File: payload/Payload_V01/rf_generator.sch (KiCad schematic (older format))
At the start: 39 parts, among them J1 Screw_Terminal_01x02, J2 Screw_Terminal_01x02, J3 Conn_Coaxial, J4 Conn_Coaxial, J5 Conn_Coaxial, U1 REF196, U2 AD9838, Y1 SG-310SCF

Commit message: added footprints and 3d models
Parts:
- JP1, JP3, JP4: footprint (none) -> Jumper:SolderJumper-3_P1.3mm_Open_Pad1.0x1.5mm
- JP2: footprint (none) -> Jumper:SolderJumper-2_P1.3mm_Bridged2Bar_Pad1.0x1.5mm
- U1: footprint (none) -> Package_SO:TSSOP-8_4.4x3mm_P0.65mm
- Y1: footprint (none) -> Crystal:Crystal_SMD_SeikoEpson_TSX3225-4Pin_3.2x2.5mm_HandSoldering
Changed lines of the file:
@@
 F 0 "JP2" H 4950 3014 50  0000 C CNN
 F 1 "Jumper" H 4950 2923 50  0000 C CNN
-F 2 "" H 4950 2750 50  0001 C CNN
+F 2 "Jumper:SolderJumper-2_P1.3mm_Bridged2Bar_Pad1.0x1.5mm" H 4950 2750 50  0001 C CNN
 F 3 "~" H 4950 2750 50  0001 C CNN
 	1    4950 2750
@@
 F 0 "JP3" H 5250 1674 50  0000 C CNN
 F 1 "Jumper_3_Open" H 5250 1583 50  0000 C CNN
-F 2 "" H 5250 1450 50  0001 C CNN
+F 2 "Jumper:SolderJumper-3_P1.3mm_Open_Pad1.0x1.5mm" H 5250 1450 50  0001 C CNN
 F 3 "~" H 5250 1450 50  0001 C CNN
 	1    5250 1450
@@
 F 0 "JP4" H 6100 1674 50  0000 C CNN
 F 1 "Jumper_3_Open" H 6100 1583 50  0000 C CNN
-F 2 "" H 6100 1450 50  0001 C CNN
+F 2 "Jumper:SolderJumper-3_P1.3mm_Open_Pad1.0x1.5mm" H 6100 1450 50  0001 C CNN
 F 3 "~" H 6100 1450 50  0001 C CNN
 	1    6100 1450
@@
 F 0 "Y1" H 3225 6125 50  0000 C CNN
 F 1 "SG-310SCF" H 3225 6034 50  0000 C CNN
-F 2 "" H 3200 5700 50  0001 C CNN
+F 2 "Crystal:Crystal_SMD_SeikoEpson_TSX3225-4Pin_3.2x2.5mm_HandSoldering" H 3200 5700 50  0001 C CNN
 F 3 "" H 3200 5700 50  0001 C CNN
 	1    3200 5700
@@
 F 0 "JP1" V 2596 5587 50  0000 L CNN
 F 1 "Jumper_3_Open" V 2505 5587 50  0000 L CNN
-F 2 "" H 2550 5500 50  0001 C CNN
+F 2 "Jumper:SolderJumper-3_P1.3mm_Open_Pad1.0x1.5mm" H 2550 5500 50  0001 C CNN
 F 3 "~" H 2550 5500 50  0001 C CNN
 	1    2550 5500
@@
 F 0 "U1" H 2644 6696 50  0000 L CNN
 F 1 "REF196" H 2350 6400 50  0000 L CNN
-F 2 "" H 2300 6600 50  0001 C CIN
+F 2 "Package_SO:TSSOP-8_4.4x3mm_P0.65mm" H 2300 6600 50  0001 C CIN
 F 3 "https://www.analog.com/static/imported-files/data_sheets/REF19xSeries.pdf" H 2300 6600 50  0001 C CIN
 	1    2300 6650

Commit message: some changes to schematics
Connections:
- net VDDA is gone; now on net +3V3: C3.1, C5.1, J1.1 (Pin_1), JP4.1 (A)
- net VDD renamed +3V3
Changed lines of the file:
@@
 Wire Wire Line
 	4750 1450 4750 1250
-$Comp
-L power:VDD #PWR?
-U 1 1 5F1B5F0C
-P 4750 1250
-AR Path="/5F1B5F0C" Ref="#PWR?"  Part="1"
-AR Path="/5F190638/5F1B5F0C" Ref="#PWR0101"  Part="1"
-F 0 "#PWR0101" H 4750 1100 50  0001 C CNN
-F 1 "VDD" H 4765 1423 50  0000 C CNN
-F 2 "" H 4750 1250 50  0001 C CNN
-F 3 "" H 4750 1250 50  0001 C CNN
-	1    4750 1250
-	1    0    0    -1
-$EndComp
 Wire Wire Line
 	5500 1450 5700 1450
@@
 Wire Wire Line
 	5850 1450 5850 1200
-$Comp
-L power:VDDA #PWR?
-U 1 1 5F1B5F1E
-P 5850 1200
-AR Path="/5F1B5F1E" Ref="#PWR?"  Part="1"
-AR Path="/5F190638/5F1B5F1E" Ref="#PWR0102"  Part="1"
-F 0 "#PWR0102" H 5850 1050 50  0001 C CNN
-F 1 "VDDA" H 5865 1373 50  0000 C CNN
-F 2 "" H 5850 1200 50  0001 C CNN
-F 3 "" H 5850 1200 50  0001 C CNN
-	1    5850 1200
-	1    0    0    -1
-$EndComp
 $Comp
 L Device:C C?
@@
 Wire Wire Line
 	9150 5700 9150 5800
-$Comp
-L power:GNDD #PWR?
-U 1 1 5F1B5FEE
-P 4650 5950
-AR Path="/5F1B5FEE" Ref="#PWR?"  Part="1"
-AR Path="/5F190638/5F1B5FEE" Ref="#PWR0114"  Part="1"
-F 0 "#PWR0114" H 4650 5700 50  0001 C CNN
-F 1 "GNDD" H 4654 5795 50  0000 C CNN
-F 2 "" H 4650 5950 50  0001 C CNN
-F 3 "" H 4650 5950 50  0001 C CNN
-	1    4650 5950
-	1    0    0    -1
-$EndComp
 Wire Wire Line
 	4650 5950 4650 5850
@@
 Wire Wire Line
 	3800 5900 3800 6000
-$Comp
-L power:GNDD #PWR?
-U 1 1 5F1B600A
-P 3800 6000
-AR Path="/5F1B600A" Ref="#PWR?"  Part="1"
-AR Path="/5F190638/5F1B600A" Ref="#PWR0115"  Part="1"
-F 0 "#PWR0115" H 3800 5750 50  0001 C CNN
-F 1 "GNDD" H 3804 5845 50  0000 C CNN
-F 2 "" H 3800 6000 50  0001 C CNN
-F 3 "" H 3800 6000 50  0001 C CNN
-	1    3800 6000
-	1    0    0    -1
-$EndComp
 Wire Wire Line
 	2900 5900 2750 5900
@@
 Wire Wire Line
 	2550 5250 2550 5150
-$Comp
-L power:VDD #PWR?
-U 1 1 5F1B6019
-P 2550 5150
-AR Path="/5F1B6019" Ref="#PWR?"  Part="1"
-AR Path="/5F190638/5F1B6019" Ref="#PWR0116"  Part="1"
-F 0 "#PWR0116" H 2550 5000 50  0001 C CNN
-F 1 "VDD" H 2565 5323 50  0000 C CNN
-F 2 "" H 2550 5150 50  0001 C CNN
-F 3 "" H 2550 5150 50  0001 C CNN
-	1    2550 5150
-	1    0    0    -1
-$EndComp
 Wire Wire Line
 	4000 5200 4250 5200
@@
 	1250 6950 1250 7050
 Connection ~ 1250 6950
-$Comp
-L power:GNDD #PWR?
-U 1 1 5F1B602F
-P 1250 7050
-AR Path="/5F1B602F" Ref="#PWR?"  Part="1"
-AR Path="/5F190638/5F1B602F" Ref="#PWR0117"  Part="1"
-F 0 "#PWR0117" H 1250 6800 50  0001 C CNN
-F 1 "GNDD" H 1254 6895 50  0000 C CNN
-F 2 "" H 1250 7050 50  0001 C CNN
-F 3 "" H 1250 7050 50  0001 C CNN
-	1    1250 7050
-	1    0    0    -1
-$EndComp
 Wire Wire Line
 	1250 6650 1500 6650
@@
 Wire Wire Line
 	2900 6950 3200 6950
-$Comp
-L power:GNDD #PWR?
-U 1 1 5F1B6046
-P 2900 7050
-AR Path="/5F1B6046" Ref="#PWR?"  Part="1"
-AR Path="/5F190638/5F1B6046" Ref="#PWR0118"  Part="1"
-F 0 "#PWR0118" H 2900 6800 50  0001 C CNN
-F 1 "GNDD" H 2904 6895 50  0000 C CNN
-F 2 "" H 2900 7050 50  0001 C CNN
-F 3 "" H 2900 7050 50  0001 C CNN
-	1    2900 7050
-	1    0    0    -1
-$EndComp
-$Comp
-L power:GNDD #PWR?
-U 1 1 5F1B604C
-P 2300 7050
-AR Path="/5F1B604C" Ref="#PWR?"  Part="1"
-AR Path="/5F190638/5F1B604C" Ref="#PWR0119"  Part="1"
-F 0 "#PWR0119" H 2300 6800 50  0001 C CNN
-F 1 "GNDD" H 2304 6895 50  0000 C CNN
-F 2 "" H 2300 7050 50  0001 C CNN
-F 3 "" H 2300 7050 50  0001 C CNN
-	1    2300 7050
-	1    0    0    -1
-$EndComp
 Wire Wire Line
 	2300 7050 2300 6950
@@
 $EndComp
 $Comp
-L power:VDD #PWR?
-U 1 1 5F1B609E
-P 1450 1200
-AR Path="/5F1B609E" Ref="#PWR?"  Part="1"
-AR Path="/5F190638/5F1B609E" Ref="#PWR0120"  Part="1"
-F 0 "#PWR0120" H 1450 1050 50  0001 C CNN
-F 1 "VDD" H 1465 1373 50  0000 C CNN
-F 2 "" H 1450 1200 50  0001 C CNN
-F 3 "" H 1450 1200 50  0001 C CNN
-	1    1450 1200
-	1    0    0    -1
-$EndComp
-$Comp
-L power:VDDA #PWR?
-U 1 1 5F1B60A4
-P 1400 2150
-AR Path="/5F1B60A4" Ref="#PWR?"  Part="1"
-AR Path="/5F190638/5F1B60A4" Ref="#PWR0121"  Part="1"
-F 0 "#PWR0121" H 1400 2000 50  0001 C CNN
-F 1 "VDDA" H 1415 2323 50  0000 C CNN
-F 2 "" H 1400 2150 50  0001 C CNN
-F 3 "" H 1400 2150 50  0001 C CNN
-	1    1400 2150
-	1    0    0    -1
-$EndComp
-$Comp
 L Device:C C?
 U 1 1 5F1B60AA
@@
 $EndComp
 $Comp
-L power:GNDD #PWR?
-U 1 1 5F1B60C2
-P 1450 1600
-AR Path="/5F1B60C2" Ref="#PWR?"  Part="1"
-AR Path="/5F190638/5F1B60C2" Ref="#PWR0122"  Part="1"
-F 0 "#PWR0122" H 1450 1350 50  0001 C CNN
-F 1 "GNDD" H 1454 1445 50  0000 C CNN
-F 2 "" H 1450 1600 50  0001 C CNN
-F 3 "" H 1450 1600 50  0001 C CNN
-	1    1450 1600
-	1    0    0    -1
-$EndComp
-$Comp
 L power:GND #PWR?
 U 1 1 5F1B60C8
@@
 	2150 1250 2700 1250
 $Comp
-L power:GNDD #PWR?
-U 1 1 5F1B60EB
-P 4150 2300
-AR Path="/5F1B60EB" Ref="#PWR?"  Part="1"
-AR Path="/5F190638/5F1B60EB" Ref="#PWR0124"  Part="1"
-F 0 "#PWR0124" H 4150 2050 50  0001 C CNN
-F 1 "GNDD" H 4154 2145 50  0000 C CNN
-F 2 "" H 4150 2300 50  0001 C CNN
-F 3 "" H 4150 2300 50  0001 C CNN
-	1    4150 2300
-	1    0    0    -1
-$EndComp
-$Comp
-L power:GNDD #PWR?
-U 1 1 5F1B60F1
-P 3900 3150
-AR Path="/5F1B60F1" Ref="#PWR?"  Part="1"
-AR Path="/5F190638/5F1B60F1" Ref="#PWR0125"  Part="1"
-F 0 "#PWR0125" H 3900 2900 50  0001 C CNN
-F 1 "GNDD" H 3904 2995 50  0000 C CNN
-F 2 "" H 3900 3150 50  0001 C CNN
-F 3 "" H 3900 3150 50  0001 C CNN
-	1    3900 3150
-	1    0    0    -1
-$EndComp
-Connection ~ 3900 3150
-$Comp
 L power:GND #PWR?
 U 1 1 5F1B60F8
@@
 Text Notes 8050 7000 0    197  ~ 39
 RF Generator
+$Comp
+L power:+3V3 #PWR?
+U 1 1 5F2F2E43
+P 2550 5150
+F 0 "#PWR?" H 2550 5000 50  0001 C CNN
+F 1 "+3V3" H 2565 5323 50  0000 C CNN
+F 2 "" H 2550 5150 50  0001 C CNN
+F 3 "" H 2550 5150 50  0001 C CNN
+	1    2550 5150
+	1    0    0    -1
+$EndComp
+$Comp
+L power:+3V3 #PWR?
+U 1 1 5F2F3260
+P 1400 2150
+F 0 "#PWR?" H 1400 2000 50  0001 C CNN
+F 1 "+3V3" H 1415 2323 50  0000 C CNN
+F 2 "" H 1400 2150 50  0001 C CNN
+F 3 "" H 1400 2150 50  0001 C CNN
+	1    1400 2150
+	1    0    0    -1
+$EndComp
+$Comp
+L power:+3V3 #PWR?
+U 1 1 5F2F483A
+P 1450 1200
+F 0 "#PWR?" H 1450 1050 50  0001 C CNN
+F 1 "+3V3" H 1465 1373 50  0000 C CNN
+F 2 "" H 1450 1200 50  0001 C CNN
+F 3 "" H 1450 1200 50  0001 C CNN
+	1    1450 1200
+	1    0    0    -1
+$EndComp
+$Comp
+L power:+3V3 #PWR?
+U 1 1 5F2F4AD5
+P 4750 1250
+F 0 "#PWR?" H 4750 1100 50  0001 C CNN
+F 1 "+3V3" H 4765 1423 50  0000 C CNN
+F 2 "" H 4750 1250 50  0001 C CNN
+F 3 "" H 4750 1250 50  0001 C CNN
+	1    4750 1250
+	1    0    0    -1
+$EndComp
+$Comp
+L power:+3V3 #PWR?
+U 1 1 5F2F4E73
+P 5850 1200
+F 0 "#PWR?" H 5850 1050 50  0001 C CNN
+F 1 "+3V3" H 5865 1373 50  0000 C CNN
+F 2 "" H 5850 1200 50  0001 C CNN
+F 3 "" H 5850 1200 50  0001 C CNN
+	1    5850 1200
+	1    0    0    -1
+$EndComp
+$Comp
+L power:GND #PWR?
+U 1 1 5F2F56C1
+P 3800 6000
+AR Path="/5F2F56C1" Ref="#PWR?"  Part="1"
+AR Path="/5F190638/5F2F56C1" Ref="#PWR?"  Part="1"
+F 0 "#PWR?" H 3800 5750 50  0001 C CNN
+F 1 "GND" H 3805 5827 50  0000 C CNN
+F 2 "" H 3800 6000 50  0001 C CNN
+F 3 "" H 3800 6000 50  0001 C CNN
+	1    3800 6000
+	1    0    0    -1
+$EndComp
+$Comp
+L power:GND #PWR?
+U 1 1 5F2F58CD
+P 2900 7050
+AR Path="/5F2F58CD" Ref="#PWR?"  Part="1"
+AR Path="/5F190638/5F2F58CD" Ref="#PWR?"  Part="1"
+F 0 "#PWR?" H 2900 6800 50  0001 C CNN
+F 1 "GND" H 2905 6877 50  0000 C CNN
+F 2 "" H 2900 7050 50  0001 C CNN
+F 3 "" H 2900 7050 50  0001 C CNN
+	1    2900 7050
+	1    0    0    -1
+$EndComp
+$Comp
+L power:GND #PWR?
+U 1 1 5F2F5C8A
+P 2300 7050
+AR Path="/5F2F5C8A" Ref="#PWR?"  Part="1"
+AR Path="/5F190638/5F2F5C8A" Ref="#PWR?"  Part="1"
+F 0 "#PWR?" H 2300 6800 50  0001 C CNN
+F 1 "GND" H 2305 6877 50  0000 C CNN
+F 2 "" H 2300 7050 50  0001 C CNN
+F 3 "" H 2300 7050 50  0001 C CNN
+	1    2300 7050
+	1    0    0    -1
+$EndComp
+$Comp
+L power:GND #PWR?
+U 1 1 5F2F5EE7
+P 1250 7050
+AR Path="/5F2F5EE7" Ref="#PWR?"  Part="1"
+AR Path="/5F190638/5F2F5EE7" Ref="#PWR?"  Part="1"
+F 0 "#PWR?" H 1250 6800 50  0001 C CNN
+F 1 "GND" H 1255 6877 50  0000 C CNN
+F 2 "" H 1250 7050 50  0001 C CNN
+F 3 "" H 1250 7050 50  0001 C CNN
+	1    1250 7050
+	1    0    0    -1
+$EndComp
+$Comp
+L power:GND #PWR?
+U 1 1 5F2F65B3
+P 4650 5950
+AR Path="/5F2F65B3" Ref="#PWR?"  Part="1"
+AR Path="/5F190638/5F2F65B3" Ref="#PWR?"  Part="1"
+F 0 "#PWR?" H 4650 5700 50  0001 C CNN
+F 1 "GND" H 4655 5777 50  0000 C CNN
+F 2 "" H 4650 5950 50  0001 C CNN
+F 3 "" H 4650 5950 50  0001 C CNN
+	1    4650 5950
+	1    0    0    -1
+$EndComp
+$Comp
+L power:GND #PWR?
+U 1 1 5F2F6675
+P 3900 3150
+AR Path="/5F2F6675" Ref="#PWR?"  Part="1"
+AR Path="/5F190638/5F2F6675" Ref="#PWR?"  Part="1"
+F 0 "#PWR?" H 3900 2900 50  0001 C CNN
+F 1 "GND" H 3905 2977 50  0000 C CNN
+F 2 "" H 3900 3150 50  0001 C CNN
+F 3 "" H 3900 3150 50  0001 C CNN
+	1    3900 3150
+	1    0    0    -1
+$EndComp
+Connection ~ 3900 3150
+$Comp
+L power:GND #PWR?
+U 1 1 5F2F6AE6
+P 4150 2300
+AR Path="/5F2F6AE6" Ref="#PWR?"  Part="1"
+AR Path="/5F190638/5F2F6AE6" Ref="#PWR?"  Part="1"
+F 0 "#PWR?" H 4150 2050 50  0001 C CNN
+F 1 "GND" H 4155 2127 50  0000 C CNN
+F 2 "" H 4150 2300 50  0001 C CNN
+F 3 "" H 4150 2300 50  0001 C CNN
+	1    4150 2300
+	1    0    0    -1
+$EndComp
+$Comp
+L power:GND #PWR?
+U 1 1 5F2F6E6D
+P 1450 1600
+AR Path="/5F2F6E6D" Ref="#PWR?"  Part="1"
+AR Path="/5F190638/5F2F6E6D" Ref="#PWR?"  Part="1"
+F 0 "#PWR?" H 1450 1350 50  0001 C CNN
+F 1 "GND" H 1455 1427 50  0000 C CNN
+F 2 "" H 1450 1600 50  0001 C CNN
+F 3 "" H 1450 1600 50  0001 C CNN
+	1    1450 1600
+	1    0    0    -1
+$EndComp
 $EndSCHEMATC

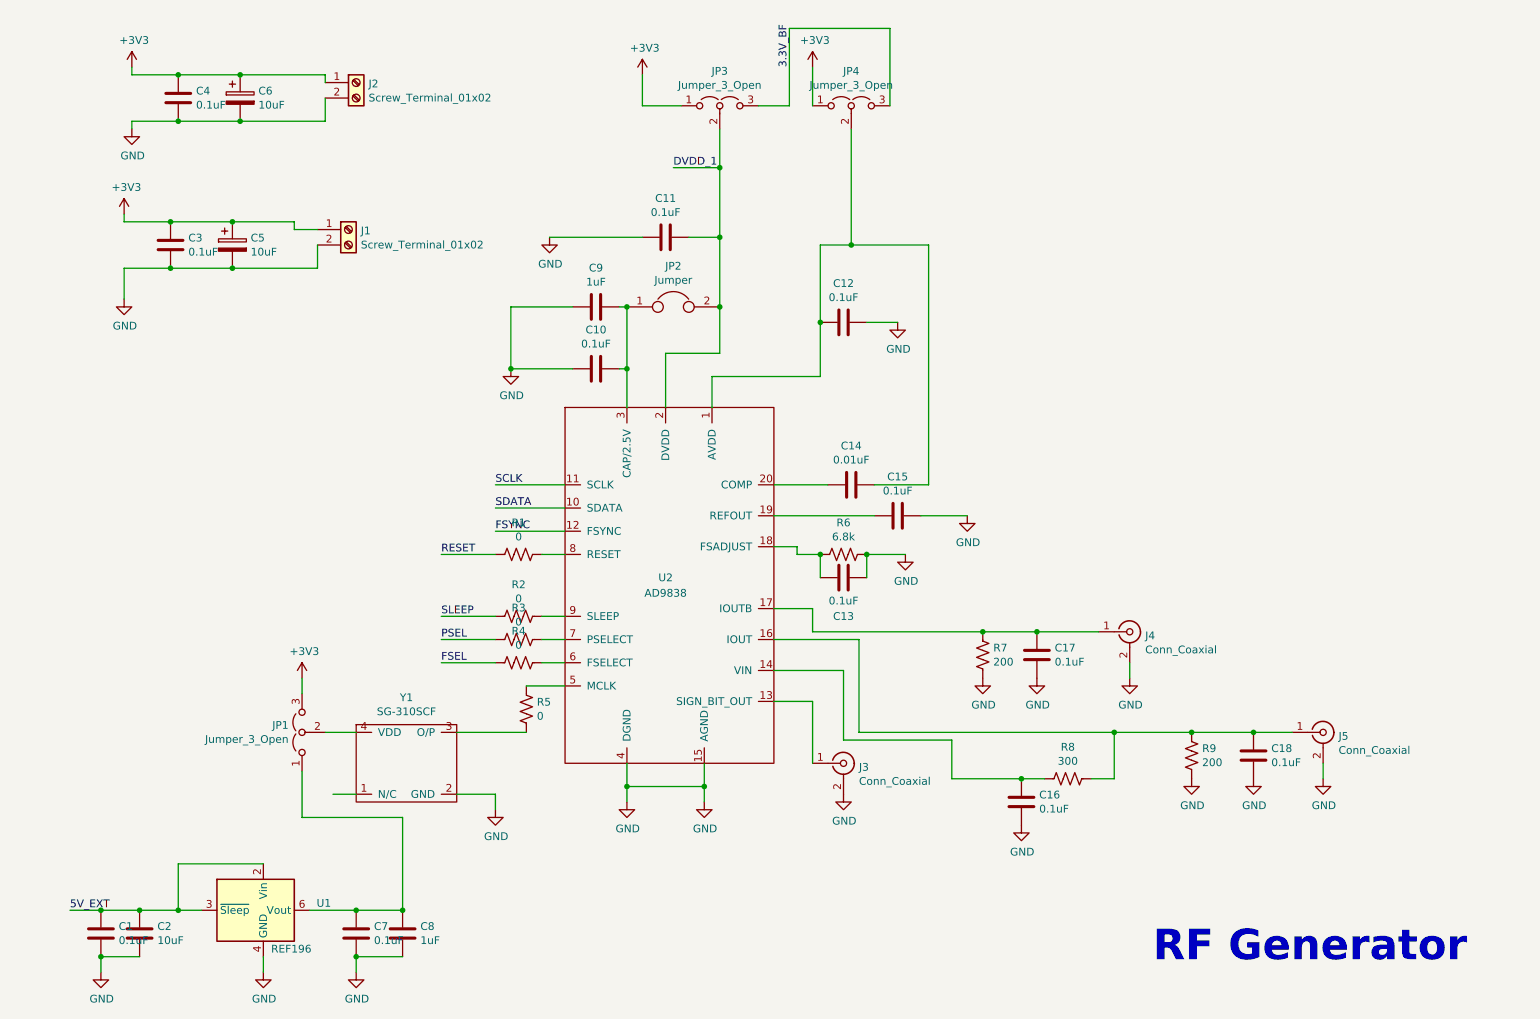
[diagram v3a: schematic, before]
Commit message: tested labels to get microcontroller working
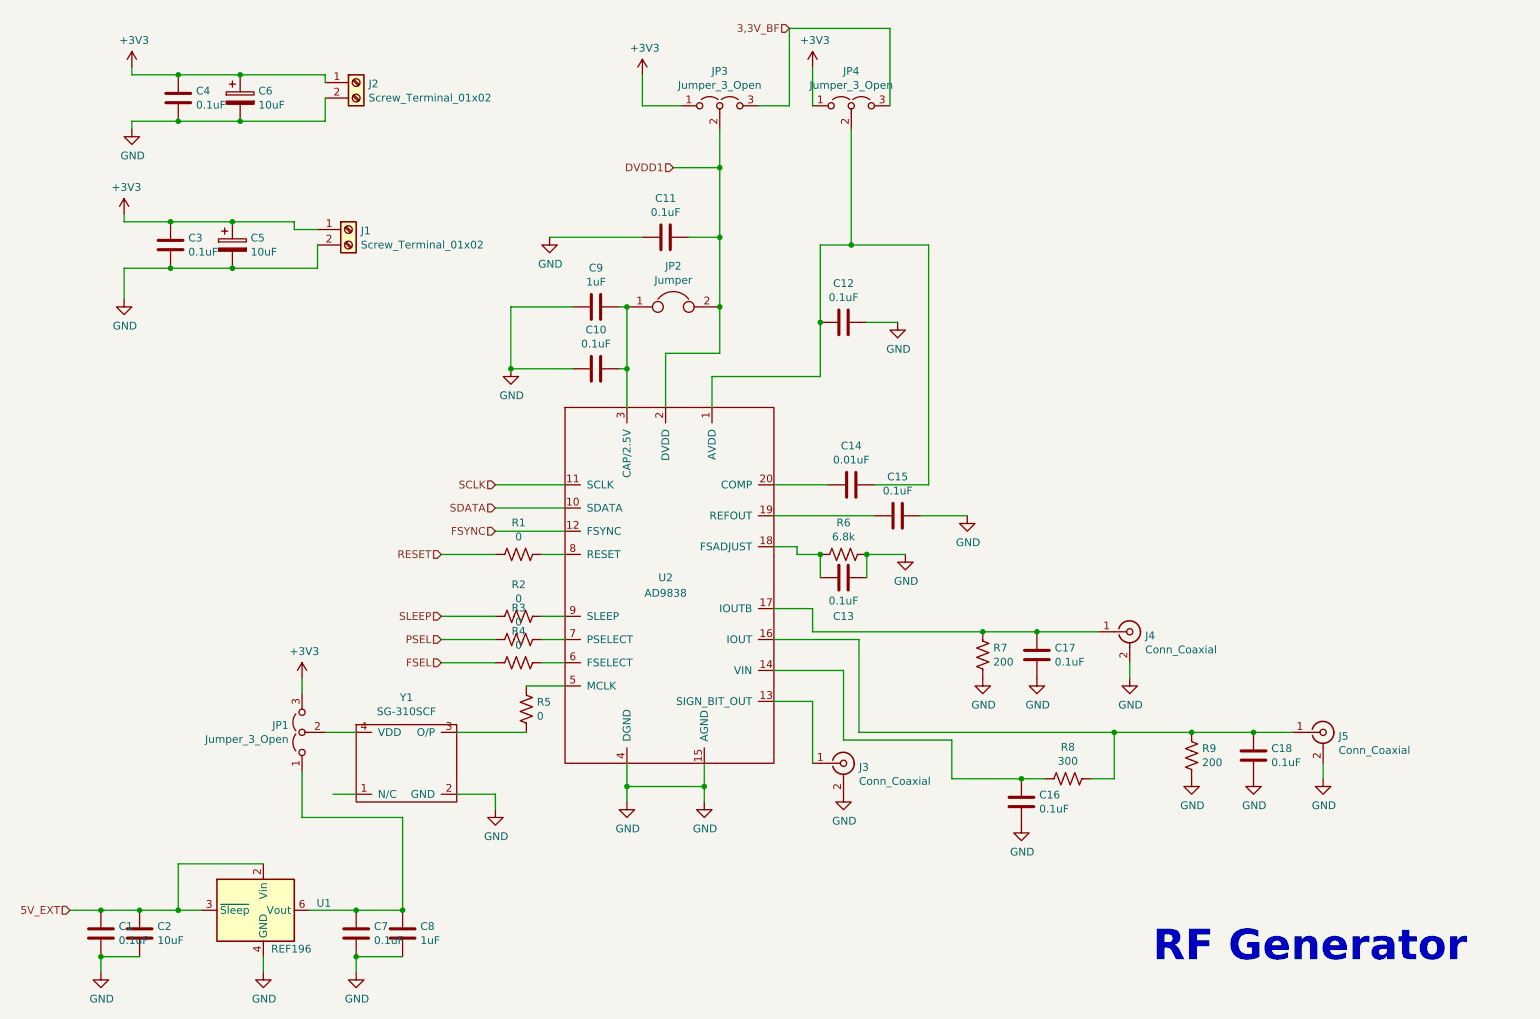
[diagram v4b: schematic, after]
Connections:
- net 3.3V_BF renamed 3,3V_BF
- net DVDD_1 renamed DVDD1
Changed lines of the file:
@@
 	5250 1850 4950 1850
 Connection ~ 5250 2300
-Text Label 4950 1850 0    50   ~ 0
-DVDD_1
 Wire Wire Line
 	5250 1850 5250 1600
@@
 Wire Wire Line
 	5700 1450 5700 950
-Text Label 5700 1200 1    50   ~ 0
-3.3V_BF
 Wire Wire Line
 	5700 950  6350 950
@@
 	1750 6650 1900 6650
 Connection ~ 1250 6650
-Text Label 1050 6650 0    50   ~ 0
-5V_EXT
 Wire Wire Line
 	2600 6650 2900 6650
@@
 Wire Wire Line
 	3800 4350 3450 4350
-Text Label 3800 3900 0    50   ~ 0
-SCLK
-Text Label 3800 4050 0    50   ~ 0
-SDATA
-Text Label 3800 4200 0    50   ~ 0
-FSYNC
-Text Label 3450 4350 0    50   ~ 0
-RESET
-Text Label 3450 4750 0    50   ~ 0
-SLEEP
-Text Label 3450 4900 0    50   ~ 0
-PSEL
-Text Label 3450 5050 0    50   ~ 0
-FSEL
 $Comp
 L Connector:Screw_Terminal_01x02 J?
@@
 	1    0    0    -1
 $EndComp
+Text HLabel 3800 3900 0    50   Input ~ 0
+SCLK
+Text HLabel 3800 4050 0    50   Input ~ 0
+SDATA
+Text HLabel 3800 4200 0    50   Input ~ 0
+FSYNC
+Text HLabel 3450 4350 0    50   Input ~ 0
+RESET
+Text HLabel 3450 4750 0    50   Input ~ 0
+SLEEP
+Text HLabel 3450 4900 0    50   Input ~ 0
+PSEL
+Text HLabel 3450 5050 0    50   Input ~ 0
+FSEL
+Text HLabel 1050 6650 0    50   Input ~ 0
+5V_EXT
+Text HLabel 4950 1850 0    50   Input ~ 0
+DVDD1
+Text HLabel 5700 950  0    50   Input ~ 0
+3,3V_BF
 $EndSCHEMATC

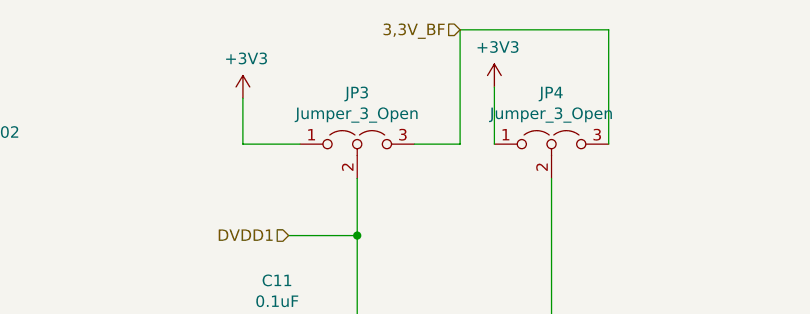
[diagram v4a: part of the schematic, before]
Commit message: added some more pins
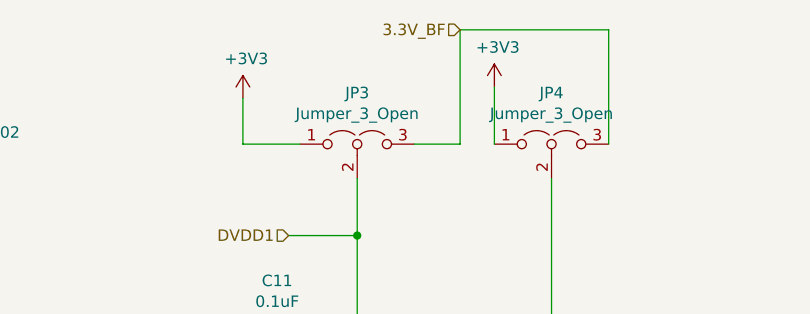
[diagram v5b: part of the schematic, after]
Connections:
- net 3,3V_BF renamed 3.3V_BF
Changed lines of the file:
@@
 DVDD1
 Text HLabel 5700 950  0    50   Input ~ 0
-3,3V_BF
+3.3V_BF
 $EndSCHEMATC
